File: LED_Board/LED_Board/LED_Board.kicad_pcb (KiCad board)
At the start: 2 copper layers, 8 parts, among them J1 Conn_01x04

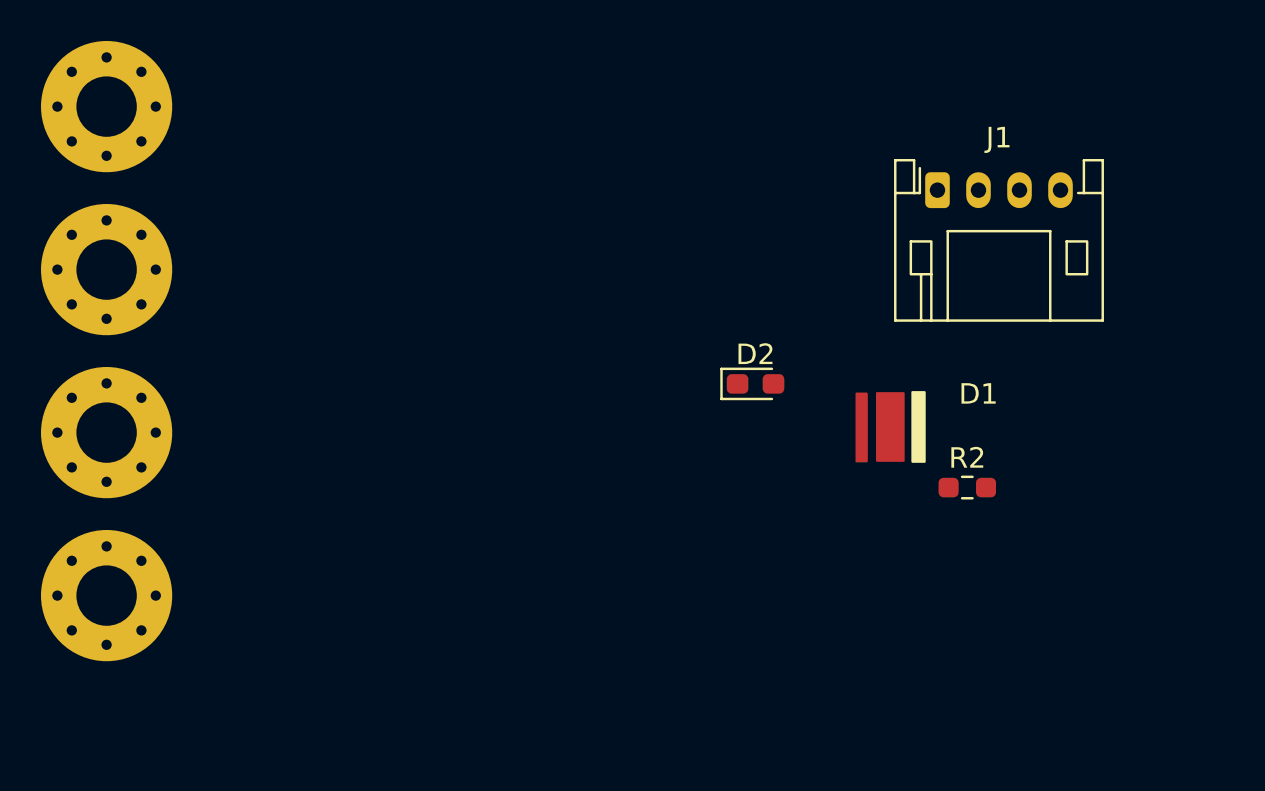
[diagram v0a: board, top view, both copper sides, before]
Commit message: Add footprint
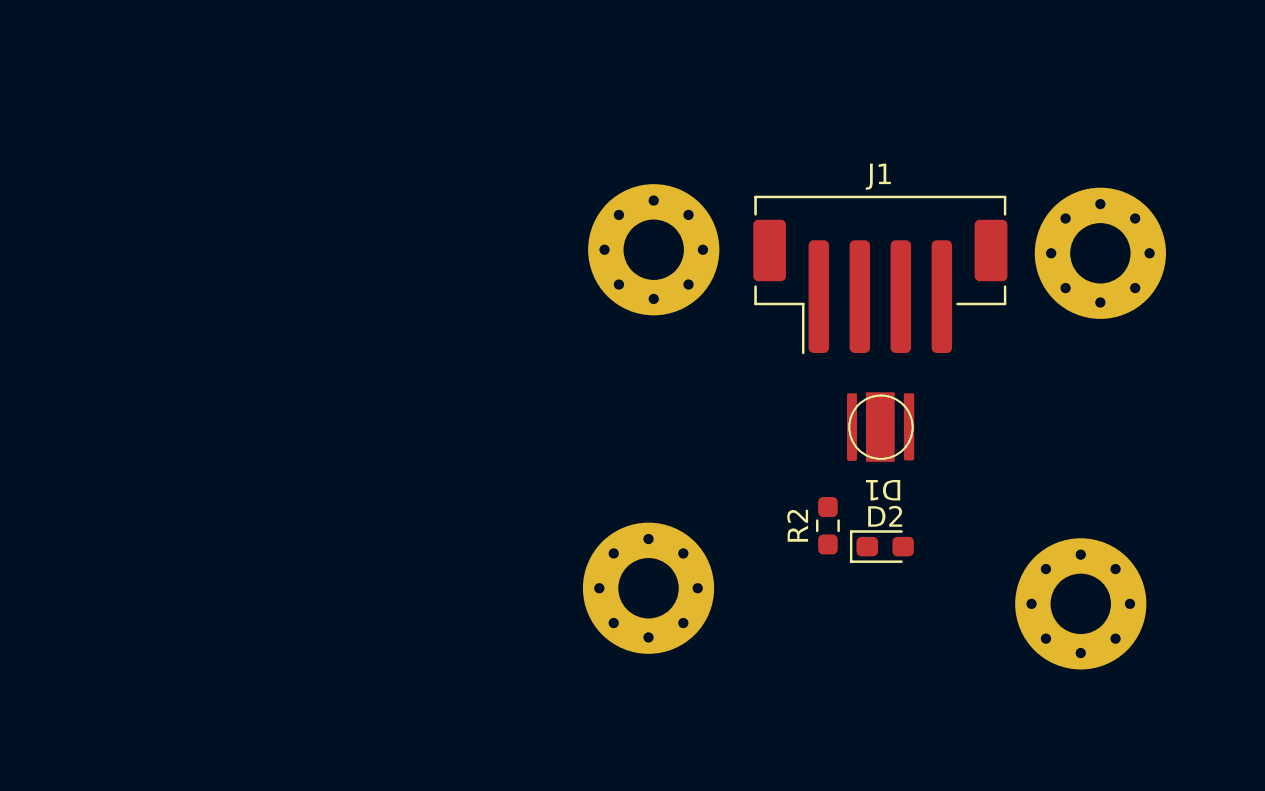
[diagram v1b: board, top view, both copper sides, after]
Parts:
- J1: footprint Connector_JST:JST_PH_S4B-PH-K_1x04_P2.00mm_Horizontal -> Connector_JST:JST_PH_B4B-PH-SM4-TB_1x04-1MP_P2.00mm_Vertical
- moved H2 48.5 mm to (181.9, 92.6)
- moved H4 47.5 mm to (181.0, 109.7)
- moved H1 27.6 mm to (160.2, 92.5)
- moved H3 27.5 mm to (159.9, 109.0)
- moved D2 10.1 mm to (171.4, 106.9)
- moved D1 9.35 mm to (171.2, 101.1), turned to 180 degrees
- moved R2 7.05 mm to (168.7, 105.9), turned to 90 degrees
- moved J1 5.46 mm to (171.2, 94.2)

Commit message: Finalized Initial Layout
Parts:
- J1: footprint Connector_JST:JST_PH_B4B-PH-SM4-TB_1x04-1MP_P2.00mm_Vertical -> Connector_JST:JST_PH_S4B-PH-SM4-TB_1x04-1MP_P2.00mm_Horizontal
- moved R2 3.48 mm to (167.6, 102.6)
- moved D2 3.24 mm to (170.8, 103.8)
- moved J1 2.42 mm to (170.9, 91.8), turned to 180 degrees
- moved H2 2.28 mm to (181.4, 90.4)
- moved H1 2.04 mm to (160.3, 90.4)
- moved D1 1.46 mm to (170.8, 99.7)
- moved H4 0.63 mm to (181.4, 109.2)
- moved H3 0.45 mm to (160.3, 109.2)
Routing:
- added copper zone on F.Cu, net GND
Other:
- board outline added: 28.2 x 26.2 mm
